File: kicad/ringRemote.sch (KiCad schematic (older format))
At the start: 24 parts, among them Y1 32.768kHz

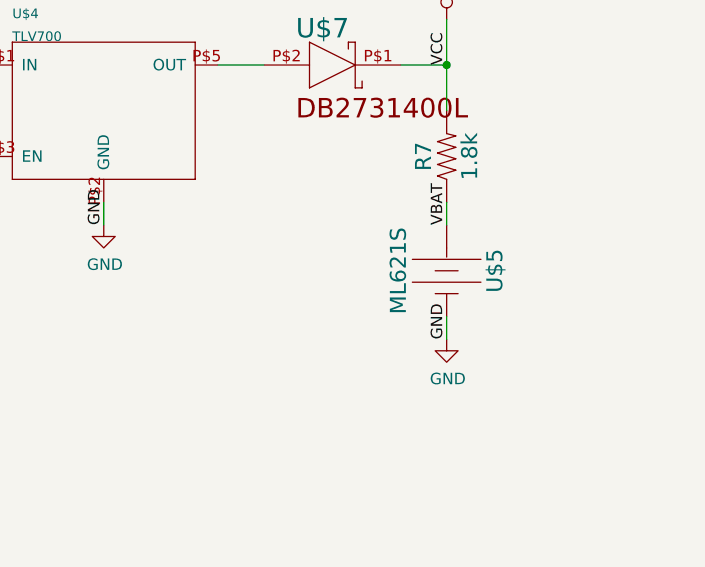
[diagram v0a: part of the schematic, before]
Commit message: finished routing main board; changed programming castellations to circular; created subschematic for battery board
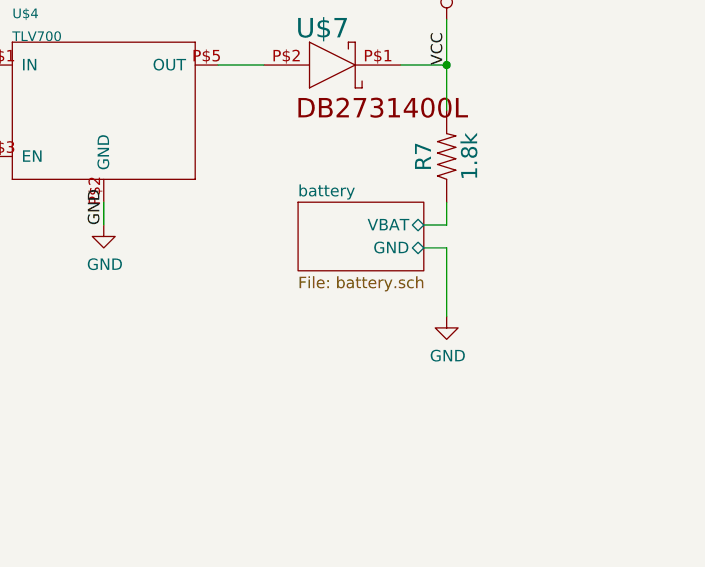
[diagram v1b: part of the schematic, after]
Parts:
- removed U$5: ML621S, ringRemote:ML621S, symbol ringRemote-eagle-import:ML621S
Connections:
- net VBAT renamed battery/VBAT
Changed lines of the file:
@@
 $Descr User 11821 8846
 encoding utf-8
-Sheet 1 1
+Sheet 1 2
 Title ""
 Date ""
@@
 GND
 Wire Wire Line
-	9800 6100 9800 6200
-Text Label 9800 6200 1    50   ~ 0
-GND
-Wire Wire Line
 	4600 2400 4700 2400
 Text Label 4700 2400 0    50   ~ 0
@@
 Text Label 4700 2300 0    50   ~ 0
 VEXT
-Wire Wire Line
-	9800 5600 9800 5700
-Text Label 9800 5700 1    50   ~ 0
-VBAT
 $Comp
 L ringRemote-eagle-import:CRYSTAL-32.768KHZSMD-3.2X1.5 Y1
@@
 	1    9800 5400
 	0    -1   -1   0
-$EndComp
-$Comp
-L ringRemote-eagle-import:ML621S U$5
-U 1 0 BCE09641
-P 9800 5900
-F 0 "U$5" H 9800 6070 70  0000 C BNN
-F 1 "ML621S" H 9800 5730 70  0000 C TNN
-F 2 "ringRemote:ML621S" H 9800 5900 50  0001 C CNN
-F 3 "" H 9800 5900 50  0001 C CNN
-	1    9800 5900
-	0    1    1    0
 $EndComp
 $Comp
@@
 $EndComp
 $Comp
-L power:GND #PWR0120
-U 1 1 5C47FF65
-P 9800 6200
-F 0 "#PWR0120" H 9800 5950 50  0001 C CNN
-F 1 "GND" H 9805 6027 50  0000 C CNN
-F 2 "" H 9800 6200 50  0001 C CNN
-F 3 "" H 9800 6200 50  0001 C CNN
-	1    9800 6200
-	1    0    0    -1
-$EndComp
-$Comp
 L power:GND #PWR0121
 U 1 1 5C480053
@@
 Text Notes 7550 4650 0    50   ~ 0
 5V must come from J3 pad of eval board;\nsupplied VCC at 2x5 swd header is NOT 5V
+$Sheet
+S 9150 5600 550  300
+U 5C488A08
+F0 "battery" 50
+F1 "battery.sch" 50
+F2 "VBAT" B R 9700 5700 50
+F3 "GND" B R 9700 5800 50
+$EndSheet
+Wire Wire Line
+	9800 5600 9800 5700
+Wire Wire Line
+	9800 5700 9700 5700
+Wire Wire Line
+	9700 5800 9800 5800
+Wire Wire Line
+	9800 5800 9800 6100
+$Comp
+L power:GND #PWR0120
+U 1 1 5C491D11
+P 9800 6100
+F 0 "#PWR0120" H 9800 5850 50  0001 C CNN
+F 1 "GND" H 9805 5927 50  0000 C CNN
+F 2 "" H 9800 6100 50  0001 C CNN
+F 3 "" H 9800 6100 50  0001 C CNN
+	1    9800 6100
+	1    0    0    -1
+$EndComp
 $EndSCHEMATC

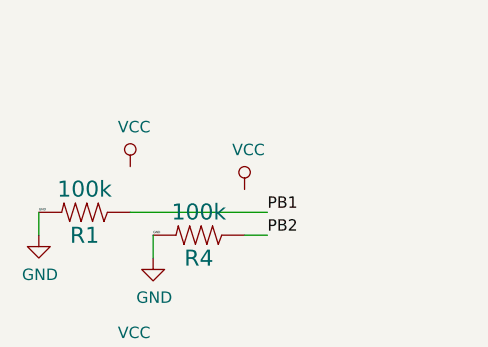
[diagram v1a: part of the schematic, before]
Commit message: finished battery board; added switch footprint to library; need to make symbol for switch and make switch board
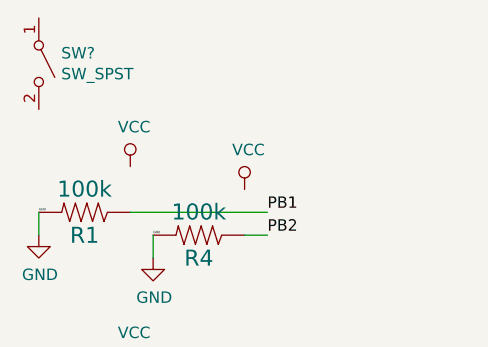
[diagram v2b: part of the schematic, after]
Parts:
- added SW?: SW_SPST, symbol Switch:SW_SPST
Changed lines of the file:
@@
 	1    0    0    -1
 $EndComp
+$Comp
+L Switch:SW_SPST SW?
+U 1 1 5C498378
+P 1700 950
+F 0 "SW?" V 1654 1048 50  0000 L CNN
+F 1 "SW_SPST" V 1745 1048 50  0000 L CNN
+F 2 "" H 1700 950 50  0001 C CNN
+F 3 "" H 1700 950 50  0001 C CNN
+	1    1700 950
+	0    1    1    0
+$EndComp
 $EndSCHEMATC

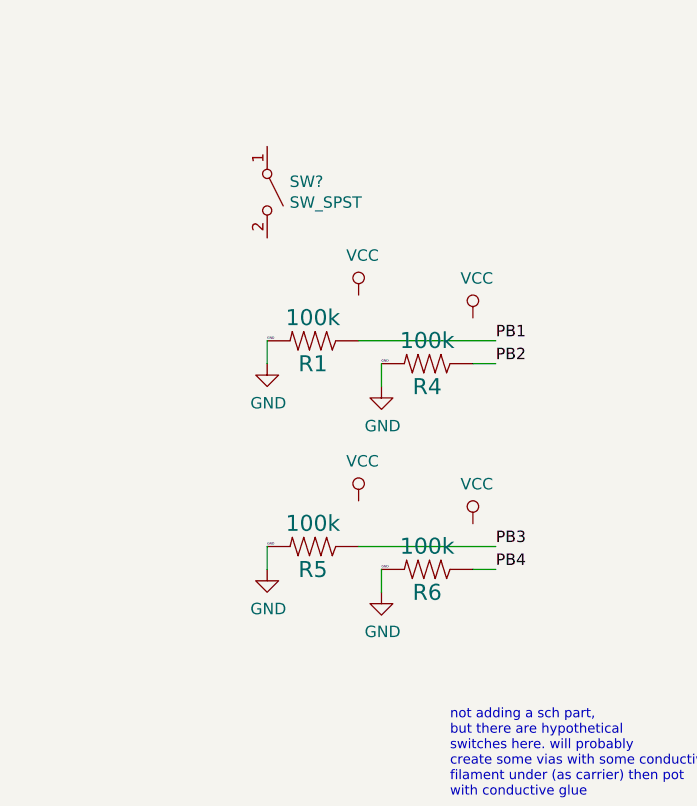
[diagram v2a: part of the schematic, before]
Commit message: added 4 pin spst switch and finished sch
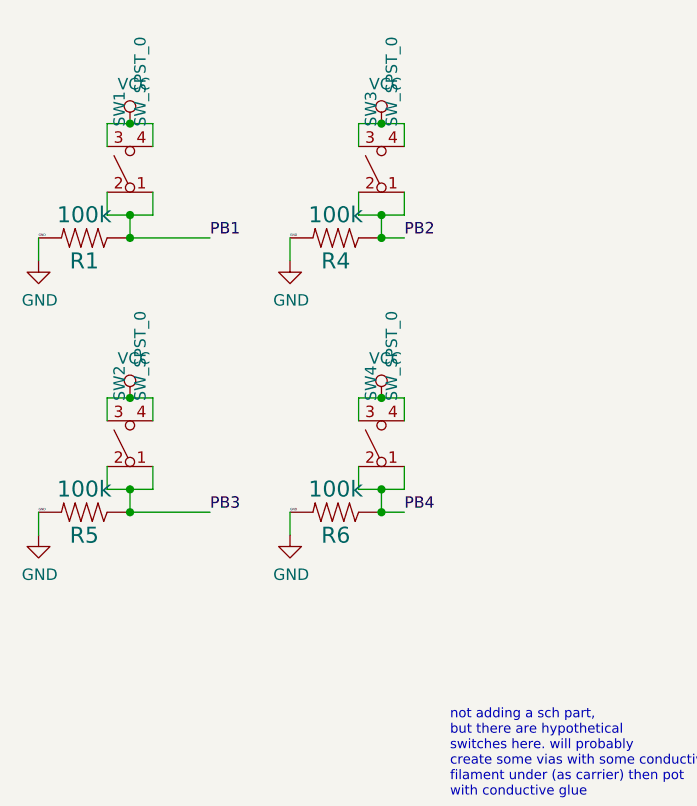
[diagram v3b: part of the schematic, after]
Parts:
- removed SW?: SW_SPST, symbol Switch:SW_SPST
- added SW1, SW2, SW3, SW4: SW_SPST_0, ringRemote:RS-187R05A2-DS MT RT, symbol ringRemote-eagle-import:SW_SPST_0
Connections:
- net PB1: now also SW1.1 (A), SW1.2 (B)
- net PB2: now also SW3.1 (A), SW3.2 (B)
- net PB3: now also SW2.1 (A), SW2.2 (B)
- net PB4: now also SW4.1 (A), SW4.2 (B)
- net VCC: now also SW1.3, SW1.4, SW2.3, SW2.4, SW3.3, SW3.4, SW4.3, SW4.4
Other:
- moved on the sheet: R1, R4, R5, R6
